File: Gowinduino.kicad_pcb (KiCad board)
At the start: 2 copper layers, 68.6 x 53.3 mm, 14 parts, among them J1 Power, J2 Analog, J3 Digital, J4 Digital, J5 SPI, J6 JTAG, U1 GW1NSR-4CQN48P, U2 W25Q32JVSS

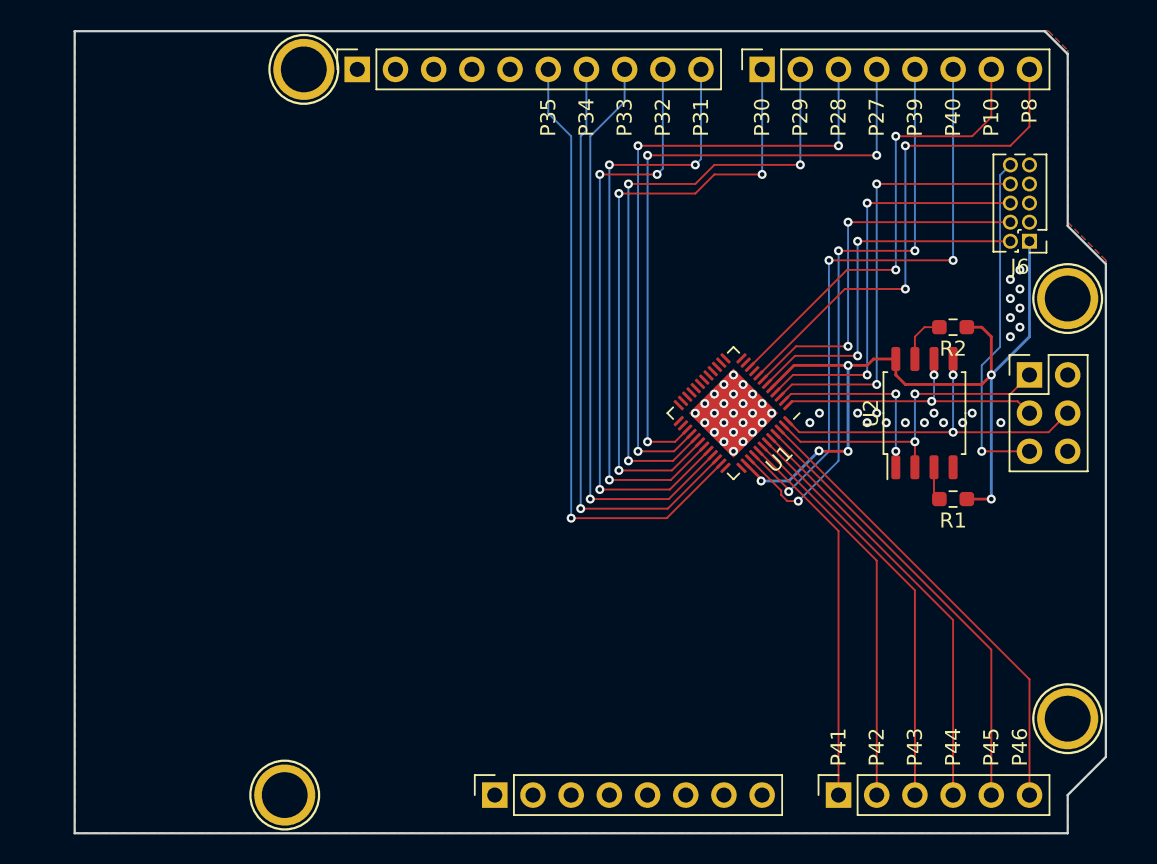
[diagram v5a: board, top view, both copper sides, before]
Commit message: Implemented the 1.8V conversion out
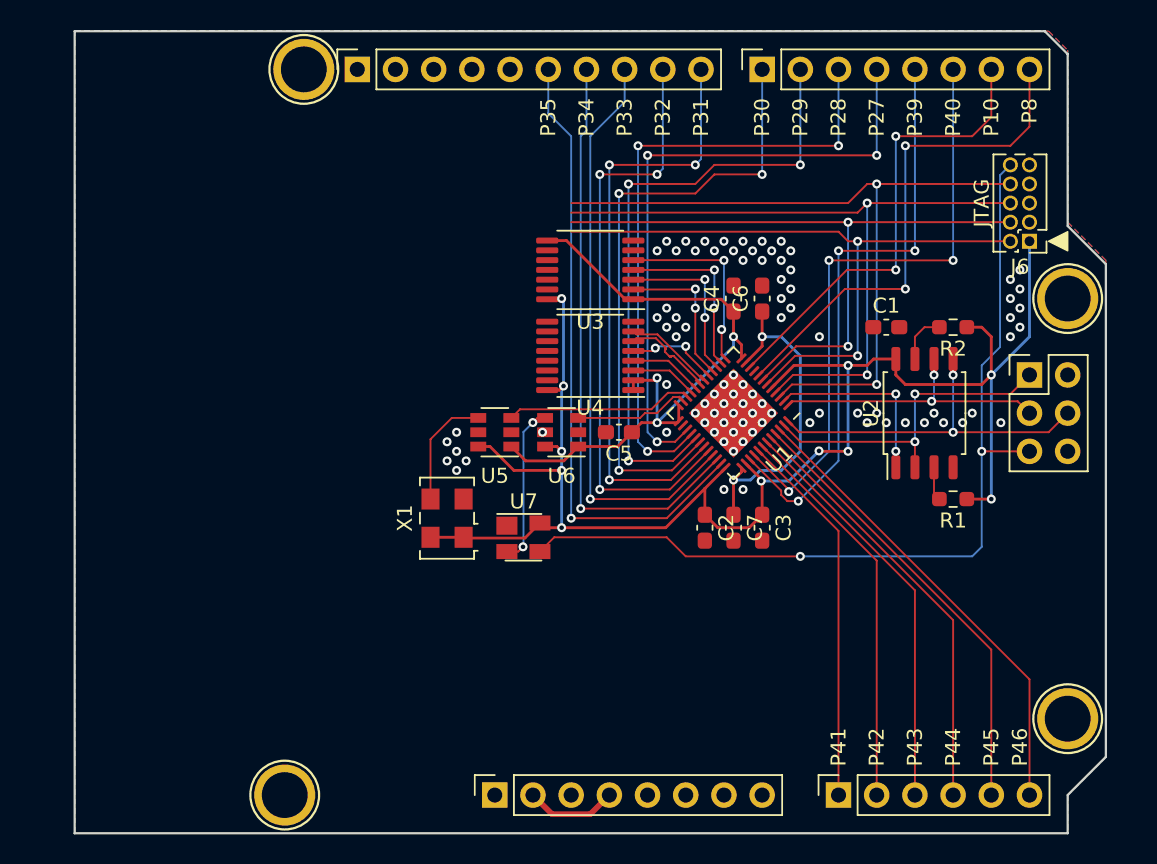
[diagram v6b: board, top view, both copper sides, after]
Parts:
- added C1: 100n, Capacitor_SMD:C_0603_1608Metric_Pad1.08x0.95mm_HandSolder, F.Cu at (165.0, 92.7)
- added C2: 100n, Capacitor_SMD:C_0603_1608Metric_Pad1.08x0.95mm_HandSolder, F.Cu at (152.9, 106.0)
- added C3: 100n, Capacitor_SMD:C_0603_1608Metric_Pad1.08x0.95mm_HandSolder, F.Cu at (156.7, 106.0)
- added C4: 100n, Capacitor_SMD:C_0603_1608Metric_Pad1.08x0.95mm_HandSolder, F.Cu at (154.8, 90.8)
- added C5: 100n, Capacitor_SMD:C_0603_1608Metric_Pad1.08x0.95mm_HandSolder, F.Cu at (147.2, 99.7)
- added C6: 100n, Capacitor_SMD:C_0603_1608Metric_Pad1.08x0.95mm_HandSolder, F.Cu at (156.7, 90.8)
- added C7: 100n, Capacitor_SMD:C_0603_1608Metric_Pad1.08x0.95mm_HandSolder, F.Cu at (154.8, 106.0)
- added U3: TXB0104PW, Package_SO:TSSOP-14_4.4x5mm_P0.65mm, F.Cu at (145.3, 88.9)
- added U4: SN74AVC4T245PW, Package_SO:TSSOP-16_4.4x5mm_P0.65mm, F.Cu at (145.3, 94.6)
- added U5: SN74LVC1T45DBV, Package_TO_SOT_SMD:SOT-23-6, F.Cu at (138.9, 99.7)
- added U6: SN74LVC1T45DBV, Package_TO_SOT_SMD:SOT-23-6, F.Cu at (143.4, 99.7)
- added U7: MAX811SEUS-T, Package_TO_SOT_SMD:SOT-143, F.Cu at (140.8, 106.7)
- added X1: 24M, Oscillator:Oscillator_SMD_EuroQuartz_XO53-4Pin_5.0x3.2mm, F.Cu at (135.8, 105.4)
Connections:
- J3 pad 1: (no net) -> /15
- J3 pad 2: (no net) -> /14
- J3 pad 5: (no net) -> /13
- U1 pad 13: (no net) -> /L13
- U1 pad 14: (no net) -> /L14
- U1 pad 15: (no net) -> /L15
- U1 pad 16: (no net) -> /LRX
- U1 pad 17: (no net) -> /LUEN
- U1 pad 18: (no net) -> /LU+
- U1 pad 19: (no net) -> /LU-
- U1 pad 20: (no net) -> /LTX
- U1 pad 21: (no net) -> /LUOE
- U1 pad 22: (no net) -> /MCLK
- U1 pad 23: (no net) -> /~RST
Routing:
- net +3V3: track 55.2 -> 116.7 mm, vias 6 -> 11
- net +1V8: track 0.00 -> 44.5 mm, vias 0 -> 3
- net /~RESET: track 23.0 -> 59.9 mm, vias 1 -> 2
- net +1V2: track 0.00 -> 21.8 mm, vias 0 -> 2
- net /TDI: track 29.0 -> 49.9 mm
- net /TDO: track 27.5 -> 47.5 mm
- net /TMS: track 24.6 -> 43.9 mm
- net /TCK: track 25.6 -> 44.1 mm
- net /L13: track 0.00 -> 12.7 mm, vias 0 -> 2
- net /MCLK: track 0.00 -> 12.5 mm
- net /L14: track 0.00 -> 11.8 mm, vias 0 -> 2
- net /L15: track 0.00 -> 10.9 mm, vias 0 -> 2
- net Net-(U6-Pad4): track 0.00 -> 10.7 mm, vias 0 -> 2
- net /LRX: track 0.00 -> 10.1 mm, vias 0 -> 2
- net /CLK24M: track 0.00 -> 7.74 mm
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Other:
- board text added: "JTAG"

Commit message: PCB: Wiring up all GPIO pins
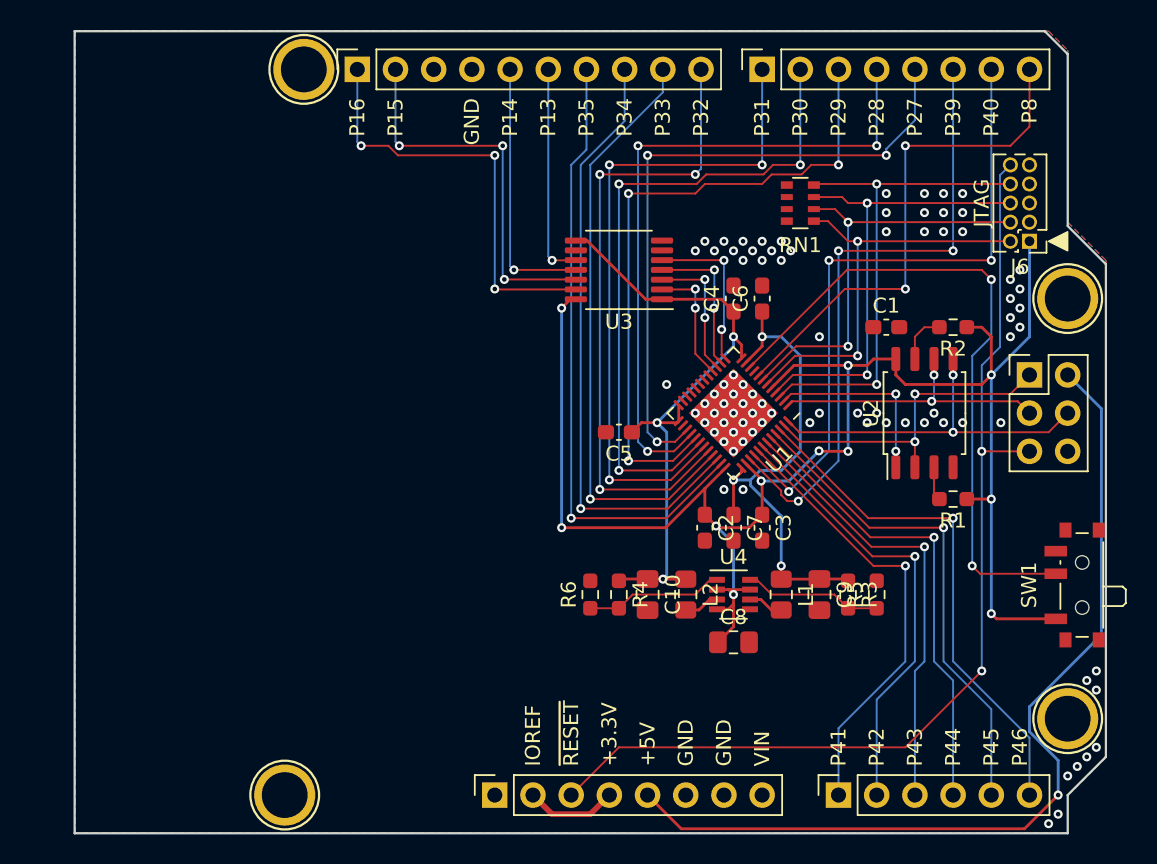
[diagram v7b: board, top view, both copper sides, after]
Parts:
- removed U5, U6: SN74LVC1T45DBV, Package_TO_SOT_SMD:SOT-23-6
- removed U7: MAX811SEUS-T, Package_TO_SOT_SMD:SOT-143
- removed X1: 24M, Oscillator:Oscillator_SMD_EuroQuartz_XO53-4Pin_5.0x3.2mm
- added C10: 22µ, Capacitor_SMD:C_0805_2012Metric_Pad1.18x1.45mm_HandSolder, F.Cu at (149.1, 110.5)
- added C8: 22µ, Capacitor_SMD:C_0805_2012Metric_Pad1.18x1.45mm_HandSolder, F.Cu at (154.8, 113.7)
- added C9: 22µ, Capacitor_SMD:C_0805_2012Metric_Pad1.18x1.45mm_HandSolder, F.Cu at (160.5, 110.5)
- added L1: 2.2µH, Inductor_SMD:L_0805_2012Metric_Pad1.15x1.40mm_HandSolder, F.Cu at (158.0, 110.5)
- added L2: 2.2µH, Inductor_SMD:L_0805_2012Metric_Pad1.15x1.40mm_HandSolder, F.Cu at (151.6, 110.5)
- added R3: 10k, Resistor_SMD:R_0603_1608Metric_Pad0.98x0.95mm_HandSolder, F.Cu at (162.4, 110.5)
- added R4: 20k, Resistor_SMD:R_0603_1608Metric_Pad0.98x0.95mm_HandSolder, F.Cu at (147.2, 110.5)
- added R5: 10k, Resistor_SMD:R_0603_1608Metric_Pad0.98x0.95mm_HandSolder, F.Cu at (164.3, 110.5)
- added R6: 10k, Resistor_SMD:R_0603_1608Metric_Pad0.98x0.95mm_HandSolder, F.Cu at (145.3, 110.5)
- added RN1: 220, Resistor_SMD:R_Array_Convex_4x0603, F.Cu at (159.3, 84.5)
- added SW1: Mode, Button_Switch_SMD:SW_SPDT_PCM12, F.Cu at (177.7, 109.9)
- U4: value SN74AVC4T245PW -> MP2122; footprint Package_SO:TSSOP-16_4.4x5mm_P0.65mm -> Package_TO_SOT_SMD:SOT-23-8
- moved U4 18.5 mm to (154.8, 110.5), turned to 0 degrees
- moved U3 1.91 mm to (147.2, 88.9)
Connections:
- U1 pad 10: /1 -> /MODE
- U1 pad 13: /L13 -> /L12
- U1 pad 14: /L14 -> /L13
- U1 pad 15: /L15 -> /L14
- U1 pad 16: /LRX -> /L15
- U1 pad 17: /LUEN -> (no net)
- U1 pad 18: /LU+ -> (no net)
- U1 pad 19: /LU- -> (no net)
- U1 pad 20: /LTX -> (no net)
- U1 pad 21: /LUOE -> (no net)
- U1 pad 22: /MCLK -> (no net)
- U1 pad 23: /~RST -> (no net)
- U1 pad 27: /4 -> /3
- U1 pad 28: /5 -> /4
- U1 pad 29: /6 -> /5
- U1 pad 30: /7 -> /6
- U1 pad 31: /8 -> /7
- U1 pad 32: /9 -> /8
- U1 pad 33: /10 -> /9
- U1 pad 34: /11 -> /10
- U1 pad 35: /12 -> /11
- U1 pad 39: /3 -> /2
- U1 pad 40: /2 -> /1
- U3 pad 10: /13 -> /12
- U3 pad 11: /14 -> /13
- U3 pad 12: /15 -> /14
- U3 pad 13: (no net) -> /15
- U3 pad 2: /LRX -> /L15
- U3 pad 3: /L15 -> /L14
- U3 pad 4: /L14 -> /L13
- U3 pad 5: /L13 -> /L12
- U4 pad 1: +1V8 -> Net-(R4-Pad2)
- U4 pad 2: +1V8 -> +3V3
- U4 pad 3: /LUOE -> Net-(L2-Pad2)
- U4 pad 4: /LTX -> +3V3
- U4 pad 5: /LUEN -> GND
- U4 pad 6: /LU- -> Net-(L1-Pad2)
- U4 pad 7: /LU+ -> +3V3
- U4 pad 8: GND -> Net-(R3-Pad2)
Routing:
- net +5V: track 0.00 -> 60.8 mm, vias 0 -> 1
- net /MODE: track 0.00 -> 44.3 mm, vias 0 -> 2
- net /15: track 0.00 -> 28.6 mm, vias 0 -> 3
- net /12: track 42.0 -> 14.4 mm
- net /14: track 0.00 -> 25.8 mm, vias 0 -> 3
- net /13: track 0.00 -> 17.6 mm, vias 0 -> 1
- net /TDI: track 49.9 -> 33.2 mm
- net /TDO: track 47.5 -> 31.2 mm
- net /TMS: track 43.9 -> 28.0 mm
- net /TCK: track 44.1 -> 28.3 mm
- net /MCLK: track 12.5 -> 0.00 mm
- net /1: track 31.3 -> 43.4 mm, vias 2 -> 3
- net +1V2: track 21.8 -> 33.8 mm, vias 2 -> 3
- net /L12: track 0.00 -> 10.8 mm, vias 0 -> 2
- net Net-(U6-Pad4): track 10.7 -> 0.00 mm, vias 2 -> 0
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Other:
- board text added: "+3.3V"
- board text added: "+5V"
- board text added: "GND"
- board text added: "IOREF"
- board text added: "P13"
- board text added: "P14"
- board text added: "P15"
- board text added: "P16"
- board text added: "VIN"
- board text added: "~RESET"
- board text removed: "P10"

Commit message: Implemented: USB and 12V VIN
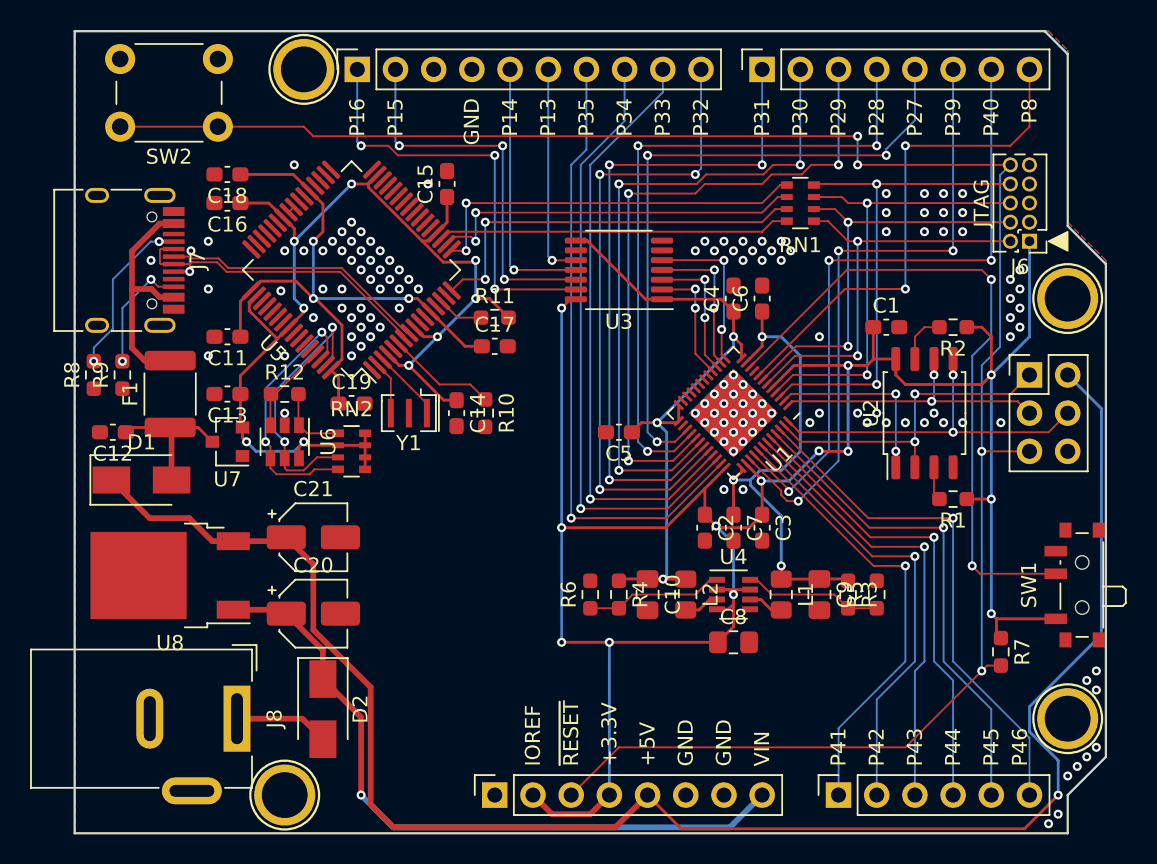
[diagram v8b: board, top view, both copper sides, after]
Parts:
- added C11: 4.7µ, Capacitor_SMD:C_0603_1608Metric_Pad1.08x0.95mm_HandSolder, F.Cu at (121.2, 93.3)
- added C12: 1µ, Capacitor_SMD:C_0603_1608Metric_Pad1.08x0.95mm_HandSolder, F.Cu at (113.5, 99.7)
- added C13: 1µ, Capacitor_SMD:C_0603_1608Metric_Pad1.08x0.95mm_HandSolder, F.Cu at (121.2, 97.2)
- added C14: 100n, Capacitor_SMD:C_0603_1608Metric_Pad1.08x0.95mm_HandSolder, F.Cu at (136.4, 98.4)
- added C15: 100n, Capacitor_SMD:C_0603_1608Metric_Pad1.08x0.95mm_HandSolder, F.Cu at (135.8, 83.2)
- added C16: 100n, Capacitor_SMD:C_0603_1608Metric_Pad1.08x0.95mm_HandSolder, F.Cu at (121.2, 84.5)
- added C17: 100n, Capacitor_SMD:C_0603_1608Metric_Pad1.08x0.95mm_HandSolder, F.Cu at (138.9, 94.0)
- added C18: 100n, Capacitor_SMD:C_0603_1608Metric_Pad1.08x0.95mm_HandSolder, F.Cu at (121.2, 82.5)
- added C19: 100n, Capacitor_SMD:C_0603_1608Metric_Pad1.08x0.95mm_HandSolder, F.Cu at (129.4, 97.8)
- added C20: 10µ, Capacitor_SMD:CP_Elec_4x4.5, F.Cu at (126.9, 111.8)
- added C21: 47µ, Capacitor_SMD:CP_Elec_4x4.5, F.Cu at (126.9, 106.7)
- added D1: SS14, Diode_SMD:D_SMA, F.Cu at (115.4, 102.9)
- added D2: M7, Diode_SMD:D_SMA, F.Cu at (127.5, 118.1)
- added F1: 1.5A, Fuse:Fuse_1812_4532Metric_Pad1.30x3.40mm_HandSolder, F.Cu at (117.3, 97.2)
- added J7: USB, Connector_USB:USB_C_Receptacle_HRO_TYPE-C-31-M-12, F.Cu at (113.5, 88.3)
- added J8: 12V, Connector_BarrelJack:BarrelJack_Wuerth_6941xx301002, F.Cu at (121.8, 118.7)
- added R10: 12k, Resistor_SMD:R_0603_1608Metric_Pad0.98x0.95mm_HandSolder, F.Cu at (138.3, 98.4)
- added R11: 1k, Resistor_SMD:R_0603_1608Metric_Pad0.98x0.95mm_HandSolder, F.Cu at (138.9, 92.1)
- added R12: 1k, Resistor_SMD:R_0603_1608Metric_Pad0.98x0.95mm_HandSolder, F.Cu at (125.0, 97.2)
- added R7: 10k, Resistor_SMD:R_0603_1608Metric_Pad0.98x0.95mm_HandSolder, F.Cu at (172.6, 114.3)
- added R8: 5.1k, Resistor_SMD:R_0603_1608Metric_Pad0.98x0.95mm_HandSolder, F.Cu at (112.3, 95.9)
- added R9: 5.1k, Resistor_SMD:R_0603_1608Metric_Pad0.98x0.95mm_HandSolder, F.Cu at (114.2, 95.9)
- added RN2: 10k, Resistor_SMD:R_Array_Convex_4x0603, F.Cu at (129.4, 101.0)
- added SW2: Reset, Button_Switch_THT:SW_PUSH_6mm, F.Cu at (120.5, 79.4)
- added U5: FT2232HL, Package_QFP:LQFP-64_10x10mm_P0.5mm, F.Cu at (129.4, 88.9)
- added U6: 93LC56B, Package_TO_SOT_SMD:SOT-23-6, F.Cu at (125.0, 100.3)
- added U7: XC6206-3.3, Package_TO_SOT_SMD:SOT-23, F.Cu at (121.2, 100.3)
- added U8: L7805, Package_TO_SOT_SMD:TO-252-2, F.Cu at (117.3, 109.2)
- added Y1: 12M, Crystal:Resonator_SMD_muRata_CSTxExxV-3Pin_3.0x1.1mm, F.Cu at (133.2, 98.4)
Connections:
- J1 pad 8: (no net) -> +12V
- RN1 pad 5: (no net) -> /JTDI
- RN1 pad 6: (no net) -> /JTDO
- RN1 pad 7: (no net) -> /JTCK
- RN1 pad 8: (no net) -> /JTMS
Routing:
- net +3.3VP: track 0.00 -> 76.5 mm, vias 0 -> 9
- net /~RESET: track 68.3 -> 131.1 mm, vias 2 -> 4
- net +5V: track 60.8 -> 114.3 mm
- net +12V: track 0.00 -> 46.2 mm, vias 0 -> 1
- net VDDF: track 0.00 -> 42.0 mm, vias 0 -> 3
- net +3V3: track 123.6 -> 155.3 mm, vias 11 -> 13
- net /JTCK: track 0.00 -> 26.8 mm, vias 0 -> 2
- net /JTDI: track 0.00 -> 26.0 mm, vias 0 -> 2
- net /JTDO: track 0.00 -> 25.3 mm, vias 0 -> 2
- net /JTMS: track 0.00 -> 23.5 mm
- net /USB Interface/D+: track 0.00 -> 20.7 mm, vias 0 -> 2
- net /USB Interface/D-: track 0.00 -> 20.3 mm
- net Net-(RN2-Pad3): track 0.00 -> 17.9 mm, vias 0 -> 2
- net Net-(RN2-Pad4): track 0.00 -> 17.7 mm, vias 0 -> 2
- net Net-(F1-Pad2): track 0.00 -> 15.9 mm
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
